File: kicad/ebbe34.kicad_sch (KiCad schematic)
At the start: 71 parts, among them U2 nice_nano

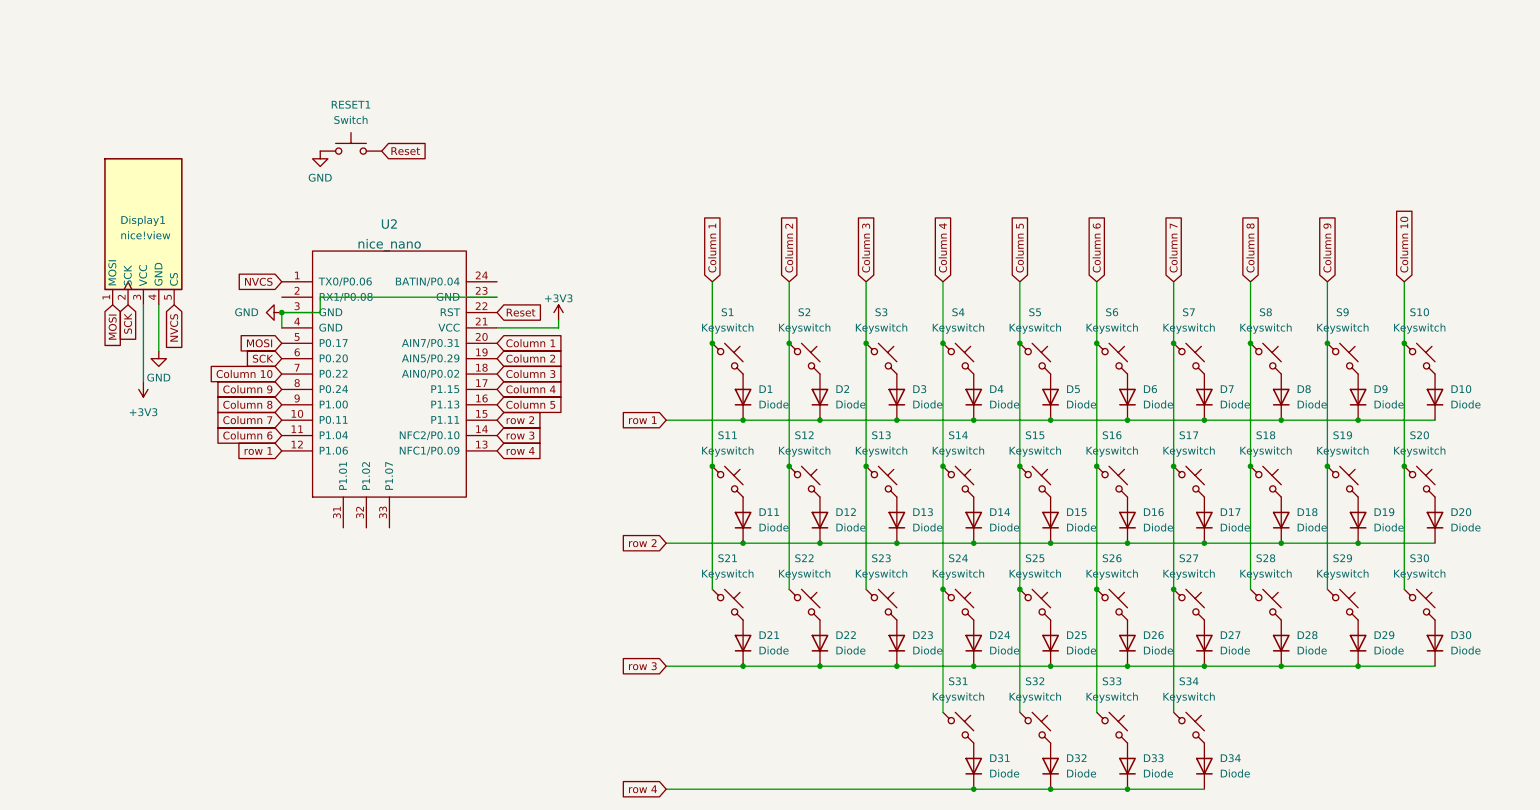
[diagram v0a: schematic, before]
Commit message: add power switch
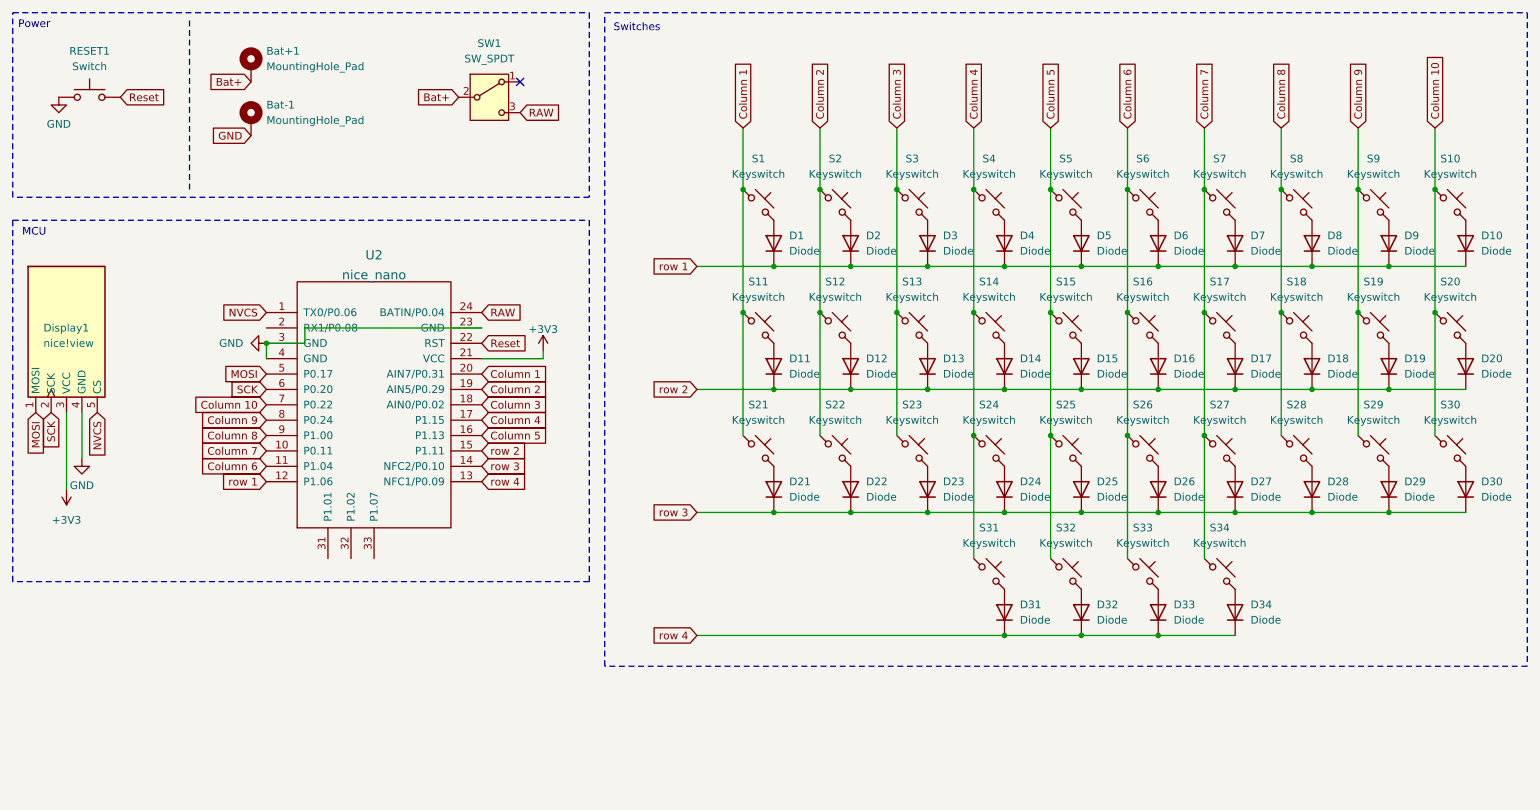
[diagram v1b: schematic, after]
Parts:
- added Bat+1: MountingHole_Pad, Library:Battery+, symbol Mechanical:MountingHole_Pad
- added Bat-1: MountingHole_Pad, Library:Battery-, symbol Mechanical:MountingHole_Pad
- added SW1: SW_SPDT, ScottoKeebs_Components:Switch_MSK12C02, symbol Switch:SW_SPDT
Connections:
- net GND: now also Bat-1.1
- net RAW: now reaches U2.24 (BATIN/P0.04)
- net RAW: now also SW1.3 (C)
- new net Bat+: Bat+1.1, SW1.2 (B)
- no-connect marks 0 -> 1
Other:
- note added: "MCU"
- note added: "Power"
- note added: "Switches"
- moved on the sheet: D1, D10, D11, D12, D13, D14, D15, D16, D17, D18, D19, D2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

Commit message: redo outline
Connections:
- net NVCS renamed CS
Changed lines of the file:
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@@
 		)
 	)
-	(global_label "NVCS"
+	(global_label "CS"
 		(shape input)
 		(at 27.94 80.01 270)
@@
 		)
 		(property "Intersheetrefs" "${INTERSHEET_REFS}"
-			(at 27.94 87.8938 90)
+			(at 27.94 85.4747 90)
 			(effects
 				(font
@@
 		)
 	)
-	(global_label "NVCS"
+	(global_label "CS"
 		(shape input)
 		(at 55.88 63.5 180)
@@
 		)
 		(property "Intersheetrefs" "${INTERSHEET_REFS}"
-			(at 48.5683 63.4206 0)
-			(effects
-				(font
+			(at 50.4153 63.5 0)
+			(effects
+				(font
